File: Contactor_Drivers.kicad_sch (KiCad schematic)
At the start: 37 parts, among them Con1 LED, Con2 LED, Con3 LED, Con4 LED, J4 Conn_01x05, J5 Conn_01x04, J6 Conn_01x04, J7 Conn_01x04, J8 Conn_01x04, Q4 IRLML0030, Q5 IRLML0030, Q6 IRLML0030, Q7 IRLML0030

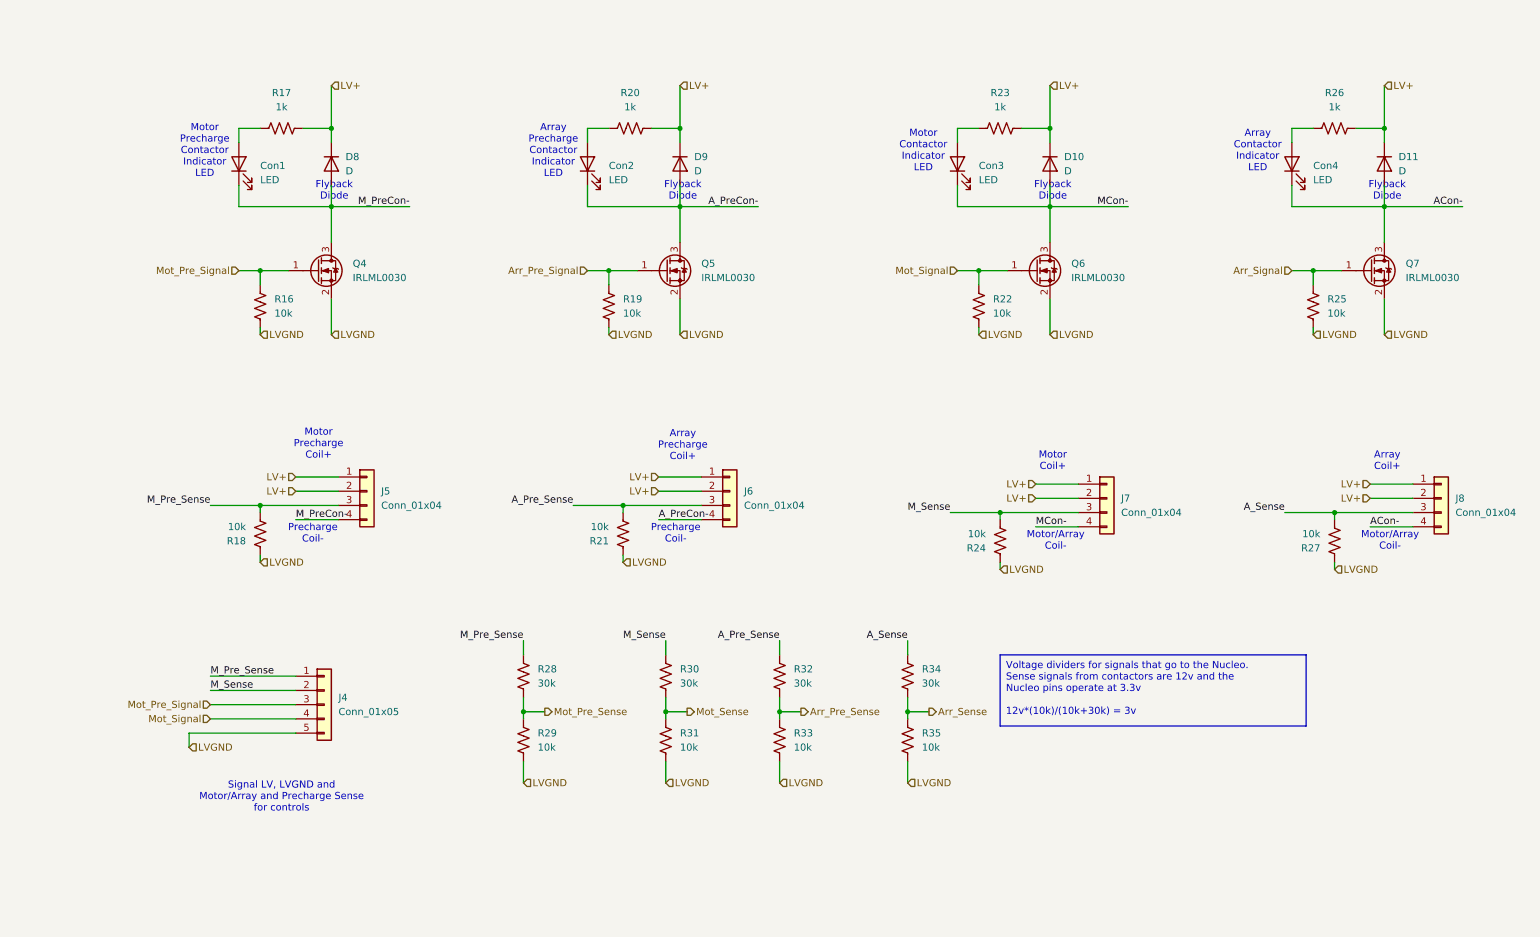
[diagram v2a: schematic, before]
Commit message: fixed lakshay and ravi comments, renamed signals to be more readable, further worked on HV side layout
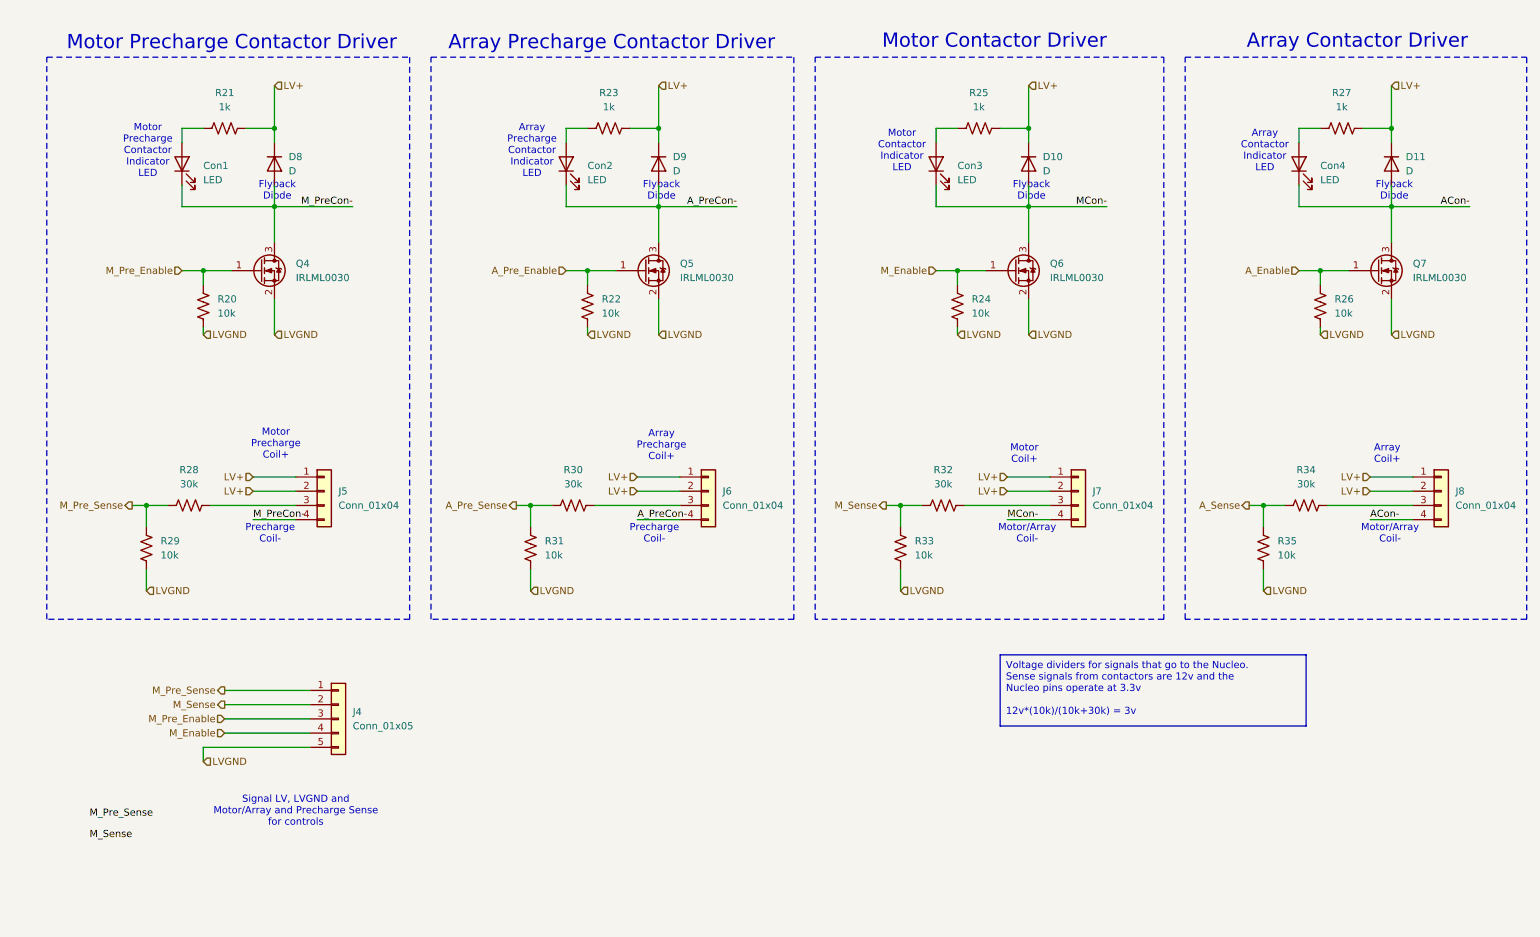
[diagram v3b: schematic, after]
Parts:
- removed R18, R21, R24, R27: 10k, Resistor_SMD:R_0805_2012Metric, symbol Device:R_US
- renumbered R16 to R20, R17 to R21, R19 to R22, R20 to R23, R22 to R24, R23 to R25, R25 to R26, R26 to R27, R32 to R30, R33 to R31, R30 to R32, R31 to R33
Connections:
- net A_Pre_Sense: now also R31.1; no longer J6.3 (Pin_3)
- net A_Sense: now also R35.1; no longer J8.3 (Pin_3)
- net M_Pre_Sense: now also R29.1; no longer J5.3 (Pin_3)
- net M_Sense: now also R33.1; no longer J7.3 (Pin_3)
- net Arr_Pre_Sense: no longer names the net of R30.2
- net Arr_Pre_Sense: now also J6.3 (Pin_3); no longer R31.1
- net Arr_Pre_Signal renamed A_Pre_Enable
- net Arr_Sense: no longer names the net of R34.2
- net Arr_Sense: now also J8.3 (Pin_3); no longer R35.1
- net Arr_Signal renamed A_Enable
- net Mot_Pre_Sense: no longer names the net of R28.2
- net Mot_Pre_Sense: now also J5.3 (Pin_3); no longer R29.1
- net Mot_Pre_Signal renamed M_Pre_Enable
- net Mot_Sense: no longer names the net of R32.2
- net Mot_Sense: now also J7.3 (Pin_3); no longer R33.1
- net Mot_Signal renamed M_Enable
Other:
- note added: "Array Contactor Driver"
- note added: "Array Precharge Contactor Driver"
- note added: "Motor Contactor Driver"
- note added: "Motor Precharge Contactor Driver"
- moved on the sheet: Con1, Con2, Con3, Con4, D10, D11, D8, D9, J4, J5, J6, J7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

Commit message: end of workday, will work on more tonight
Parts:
- removed J4: Conn_01x05, utsvt-conn:Molex_MicroFit_01x06_Horizontal, symbol Connector_Generic:Conn_01x05
- added A_Pre_Sen_TP1, A_Sen_TP2, M_Pre_Sen_TP1, M_Sen_TP1: TestPoint, utsvt-special:TestPoint_HEX_3mmID, symbol Connector:TestPoint
- renumbered J5 to J4, J6 to J5, J7 to J6, J8 to J7
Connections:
- net ACon-: now also J7.1 (Pin_1); no longer J7.4 (Pin_4)
- net A_PreCon-: now also J5.1 (Pin_1); no longer J5.4 (Pin_4)
- net A_Pre_Sense: now also A_Pre_Sen_TP1.1
- net A_Sense: now also A_Sen_TP2.1
- net LV+: now also J4.3 (Pin_3), J4.4 (Pin_4), J5.3 (Pin_3), J5.4 (Pin_4), J6.3 (Pin_3), J6.4 (Pin_4), J7.3 (Pin_3), J7.4 (Pin_4); no longer J4.1 (Pin_1), J4.2 (Pin_2), J5.1 (Pin_1), J5.2 (Pin_2), J6.1 (Pin_1), J6.2 (Pin_2), J7.1 (Pin_1), J7.2 (Pin_2)
- net MCon-: now also J6.1 (Pin_1); no longer J6.4 (Pin_4)
- net M_PreCon-: now also J4.1 (Pin_1); no longer J4.4 (Pin_4)
- net M_Pre_Sense: now also M_Pre_Sen_TP1.1
- net M_Sense: now also M_Sen_TP1.1
- net at R28.2: now also J4.2 (Pin_2); no longer J4.3 (Pin_3)
- net at R34.2: now also J7.2 (Pin_2); no longer J7.3 (Pin_3)
- net at R32.2: now also J6.2 (Pin_2); no longer J6.3 (Pin_3)
- net at R30.2: now also J5.2 (Pin_2); no longer J5.3 (Pin_3)
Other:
- note removed: "Signal LV, LVGND and Motor/Array and Precharge Sense for controls"

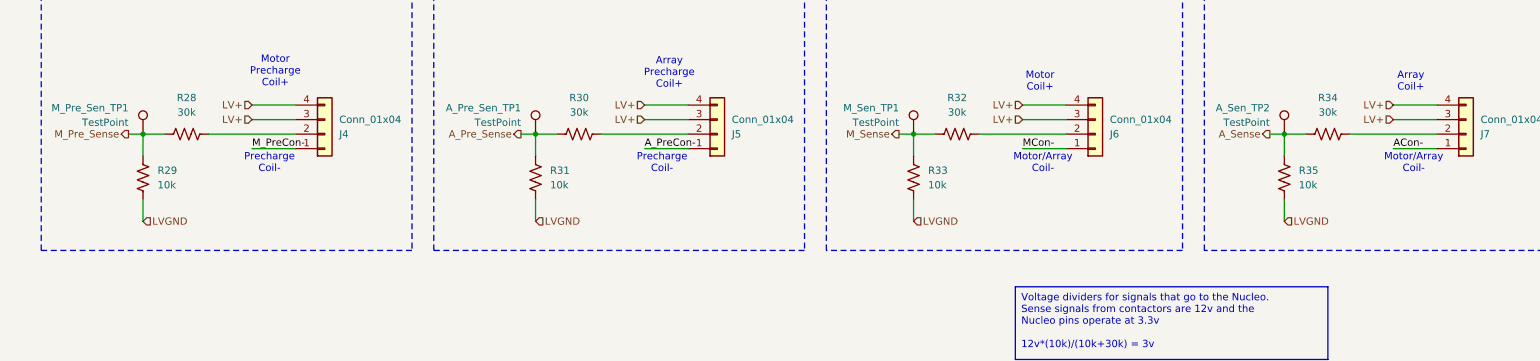
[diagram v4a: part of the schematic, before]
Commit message: added debounce caps to sense pins of contactors
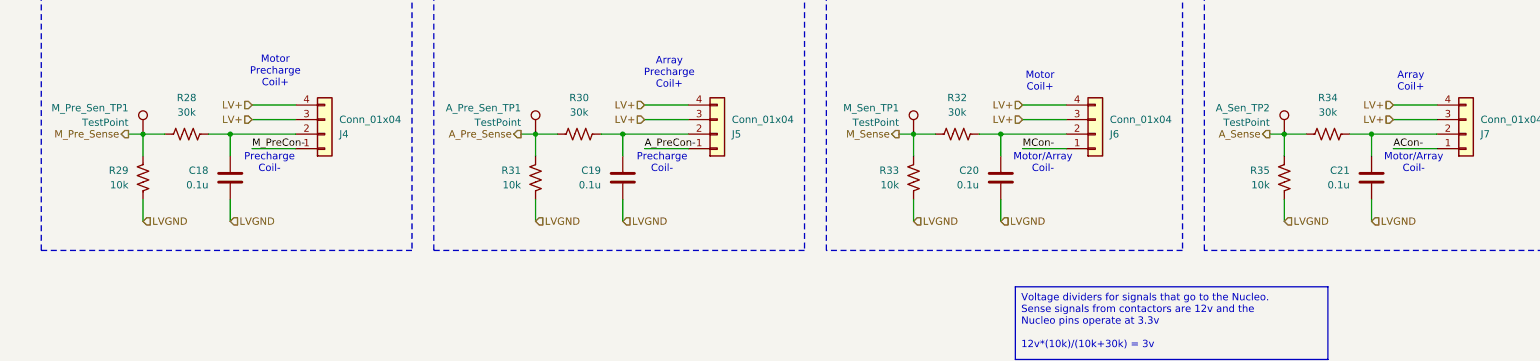
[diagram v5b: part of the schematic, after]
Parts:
- added C18, C19, C20, C21: 0.1u, Capacitor_SMD:C_0805_2012Metric, symbol Device:C
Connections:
- net LVGND: now also C18.2, C19.2, C20.2, C21.2
- net at J4.2 (Pin_2), R28.2: now also C18.1
- net at J7.2 (Pin_2), R34.2: now also C21.1
- net at J6.2 (Pin_2), R32.2: now also C20.1
- net at J5.2 (Pin_2), R30.2: now also C19.1

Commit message: initial commit v2
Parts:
- removed A_Sen_TP2: TestPoint, utsvt-special:TestPoint_HEX_3mmID, symbol Connector:TestPoint
- removed C21: 0.1u, Capacitor_SMD:C_0805_2012Metric, symbol Device:C
- removed Con4: LED, LED_SMD:LED_0805_2012Metric, symbol Device:LED
- removed D11: D, Active-PrechargeLib:SODFL4724X108N, symbol Device:D
- removed J7: Conn_01x04, utsvt-conn:Molex_MicroFit3.0_1x4xP3.00mm_PolarizingPeg_Vertical, symbol Connector_Generic:Conn_01x04
- removed Q7: IRLML0030, Package_TO_SOT_SMD:SOT-23, symbol Transistor_FET:IRLML0030
- removed R26, R35: 10k, Resistor_SMD:R_0805_2012Metric, symbol Device:R_US
- removed R27: 1k, Resistor_SMD:R_0805_2012Metric, symbol Device:R_US
- removed R34: 30k, Resistor_SMD:R_0805_2012Metric, symbol Device:R_US
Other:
- note removed: "Array Coil+"
- note removed: "Array Contactor Driver"
- note removed: "Array Contactor Indicator LED"
- moved on the sheet: A_Pre_Sen_TP1, C18, C19, C20, Con1, Con2, Con3, D10, D8, D9, J4, J5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

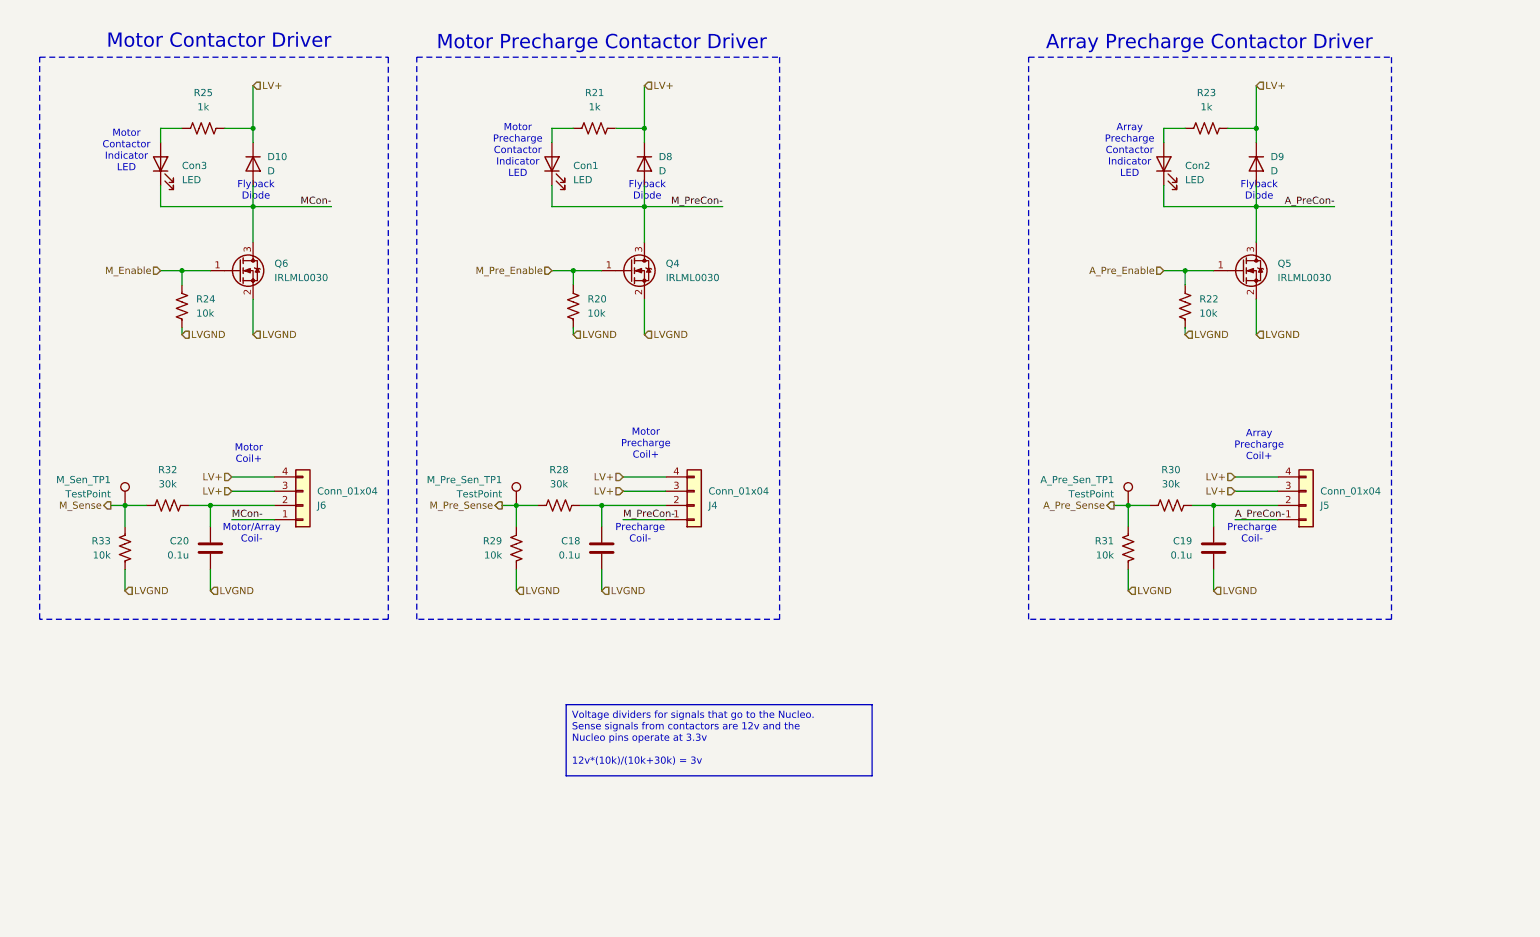
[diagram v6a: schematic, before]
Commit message: fixed HV layout and added the both nmos
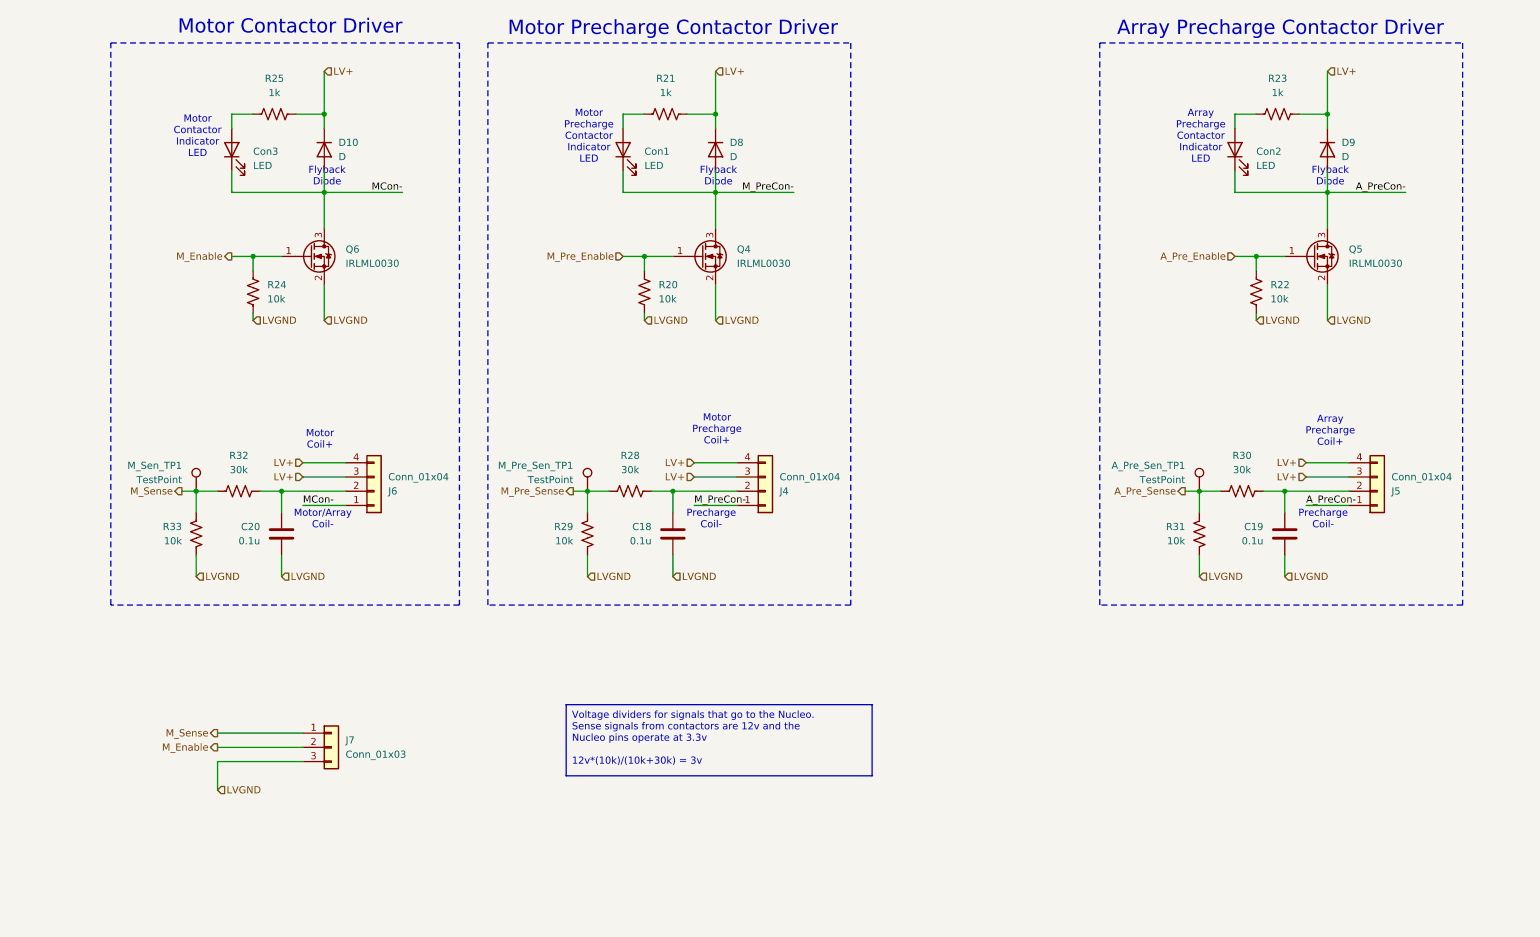
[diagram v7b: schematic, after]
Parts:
- added J7: Conn_01x03, utsvt-conn:Molex_MicroFit3.0_1x3xP3.00mm_PolarizingPeg_Vertical, symbol Connector_Generic:Conn_01x03
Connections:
- net LVGND: now also J7.3 (Pin_3)
- net M_Enable: now also J7.2 (Pin_2)
- net M_Sense: now also J7.1 (Pin_1)
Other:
- moved on the sheet: A_Pre_Sen_TP1, C18, C19, C20, Con1, Con2, Con3, D10, D8, D9, J4, J5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

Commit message: oops forgot to push workday changes 3/8/25
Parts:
- removed J7: Conn_01x03, utsvt-conn:Molex_MicroFit3.0_1x3xP3.00mm_PolarizingPeg_Vertical, symbol Connector_Generic:Conn_01x03
- added J7: Conn_01x04, utsvt-conn:Molex_MicroFit3.0_1x4xP3.00mm_PolarizingPeg_Vertical, symbol Connector_Generic:Conn_01x04
- added R26: R_US, Resistor_SMD:R_0805_2012Metric, symbol Device:R_US
- added U8: VOS618A, Package_SO:SOP-4_4.4x2.6mm_P1.27mm, symbol Isolator:VOS618A
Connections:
- net LV+: now also J7.2 (Pin_2)
- net LVGND: now also U8.2
- net M_Enable: now also J7.1 (Pin_1)
- net M_Sense: now also R26.1
- new net: R26.2, U8.1
- new net AUX+: J7.3 (Pin_3), U8.4
- new net AUX-: J7.4 (Pin_4), U8.3
